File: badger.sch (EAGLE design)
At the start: 6 parts, among them U1 NCP1402

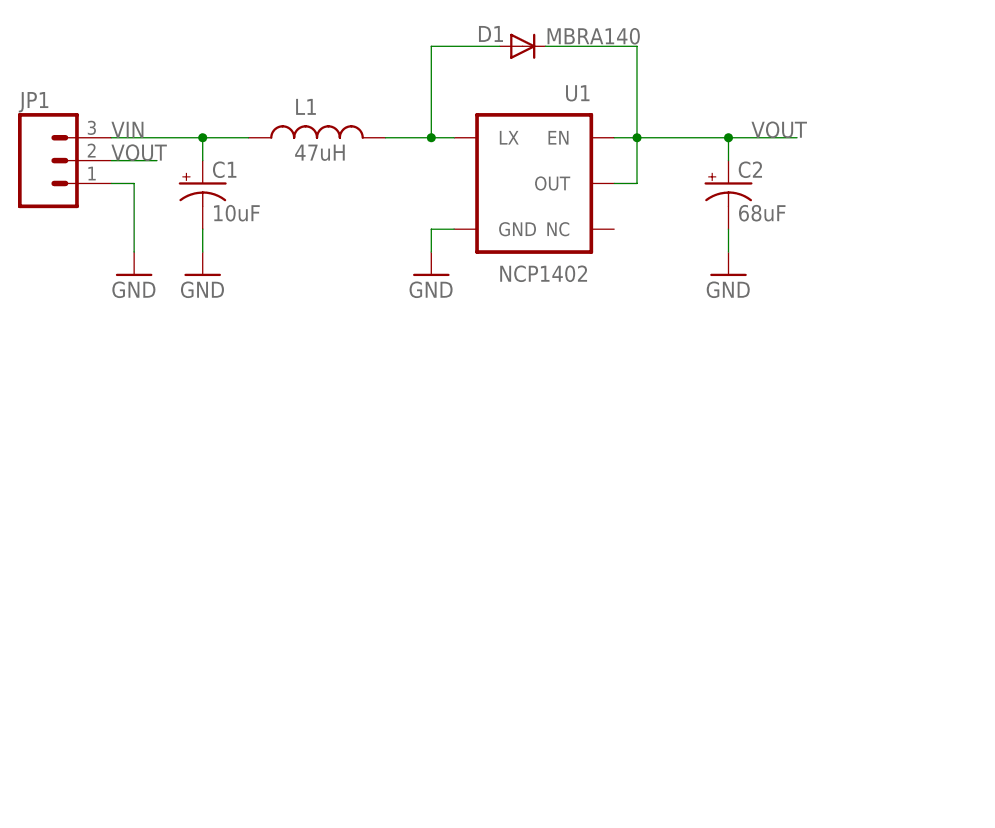
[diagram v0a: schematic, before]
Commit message: add esp8266 lib and add part
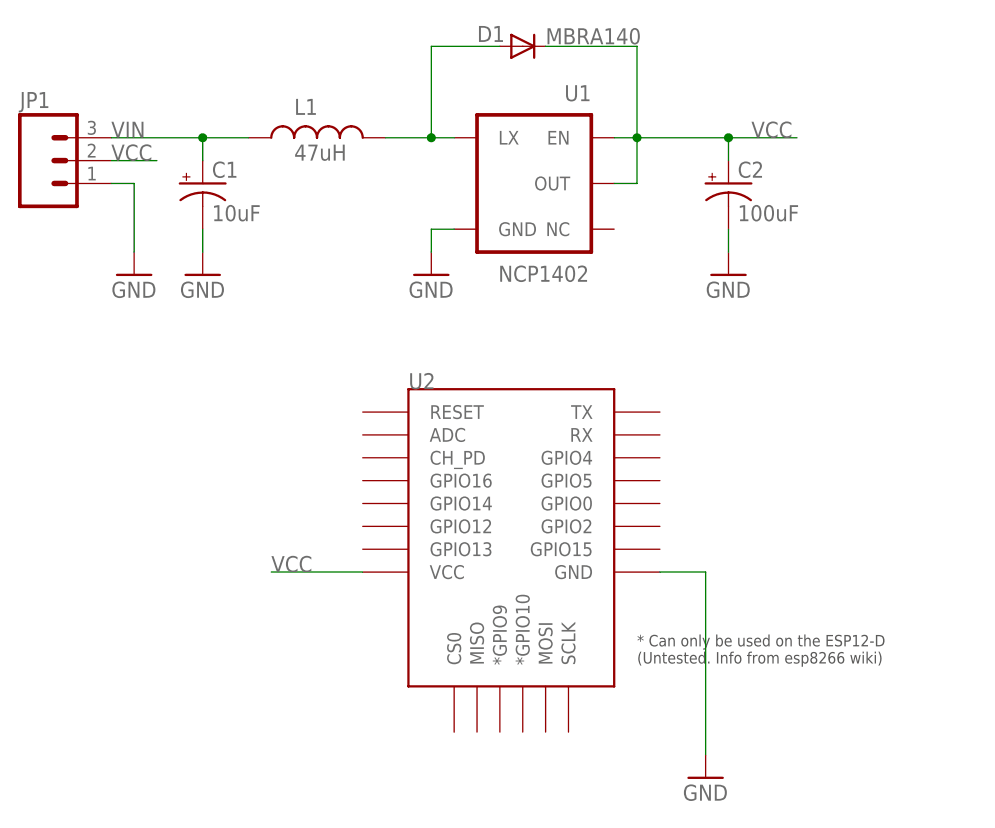
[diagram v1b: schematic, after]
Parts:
- added U2: (no value), esp8266modules:ESP12ESMD
- C2: value 68uF -> 100uF
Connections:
- removed net VOUT: C2.+, D1.C, JP1.2, U1.EN, U1.OUT
- new net VCC: C2.+, D1.C, JP1.2, U1.EN, U1.OUT, U2.VCC
- net GND: now also U2.GND
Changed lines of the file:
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@@
 <part name="D1" library="SparkFun" deviceset="DIODE" device="SMA" value="MBRA140"/>
 <part name="C1" library="SparkFun" deviceset="CAP_POL" device="1206" value="10uF"/>
-<part name="C2" library="SparkFun" deviceset="CAP_POL" device="3528" value="68uF"/>
+<part name="C2" library="SparkFun" deviceset="CAP_POL" device="3528" value="100uF"/>
 <part name="L1" library="SparkFun" deviceset="INDUCTOR" device="CR54" value="47uH"/>
 <part name="GND1" library="SparkFun" deviceset="GND" device=""/>
@@
 <part name="GND3" library="SparkFun" deviceset="GND" device=""/>
 <part name="GND4" library="SparkFun" deviceset="GND" device=""/>
+<part name="U2" library="esp8266modules" deviceset="ESP12E" device="SMD"/>
+<part name="GND5" library="SparkFun" deviceset="GND" device=""/>
 </parts>
 <sheets>
@@
 <instance part="GND3" gate="1" x="45.72" y="48.26"/>
 <instance part="GND4" gate="1" x="78.74" y="48.26"/>
+<instance part="U2" gate="G$1" x="55.88" y="25.4"/>
+<instance part="GND5" gate="1" x="76.2" y="-7.62"/>
 </instances>
 <busses>
@@
 <pinref part="D1" gate="G$1" pin="A"/>
 <pinref part="L1" gate="G$1" pin="2"/>
-</segment>
-</net>
-<net name="VOUT" class="0">
-<segment>
-<wire x1="66.04" y1="63.5" x2="68.58" y2="63.5" width="0.1524" layer="91"/>
-<wire x1="68.58" y1="63.5" x2="68.58" y2="58.42" width="0.1524" layer="91"/>
-<wire x1="68.58" y1="58.42" x2="66.04" y2="58.42" width="0.1524" layer="91"/>
-<wire x1="58.42" y1="73.66" x2="68.58" y2="73.66" width="0.1524" layer="91"/>
-<wire x1="68.58" y1="73.66" x2="68.58" y2="63.5" width="0.1524" layer="91"/>
-<wire x1="68.58" y1="63.5" x2="78.74" y2="63.5" width="0.1524" layer="91"/>
-<wire x1="78.74" y1="63.5" x2="78.74" y2="60.96" width="0.1524" layer="91"/>
-<wire x1="78.74" y1="63.5" x2="86.36" y2="63.5" width="0.1524" layer="91"/>
-<junction x="68.58" y="63.5"/>
-<junction x="78.74" y="63.5"/>
-<label x="81.28" y="63.5" size="1.778" layer="95"/>
-<pinref part="U1" gate="G$1" pin="EN"/>
-<pinref part="U1" gate="G$1" pin="OUT"/>
-<pinref part="D1" gate="G$1" pin="C"/>
-<pinref part="C2" gate="G$1" pin="+"/>
-</segment>
-<segment>
-<wire x1="10.16" y1="60.96" x2="15.24" y2="60.96" width="0.1524" layer="91"/>
-<label x="10.16" y="60.96" size="1.778" layer="95"/>
-<pinref part="JP1" gate="G$1" pin="2"/>
 </segment>
 </net>
@@
 <pinref part="GND1" gate="1" pin="GND"/>
 </segment>
+<segment>
+<pinref part="U2" gate="G$1" pin="GND"/>
+<pinref part="GND5" gate="1" pin="GND"/>
+<wire x1="71.12" y1="15.24" x2="76.2" y2="15.24" width="0.1524" layer="91"/>
+<wire x1="76.2" y1="15.24" x2="76.2" y2="-5.08" width="0.1524" layer="91"/>
+</segment>
 </net>
 <net name="VIN" class="0">
@@
 </segment>
 </net>
+<net name="VCC" class="0">
+<segment>
+<wire x1="66.04" y1="63.5" x2="68.58" y2="63.5" width="0.1524" layer="91"/>
+<wire x1="68.58" y1="63.5" x2="68.58" y2="58.42" width="0.1524" layer="91"/>
+<wire x1="68.58" y1="58.42" x2="66.04" y2="58.42" width="0.1524" layer="91"/>
+<wire x1="58.42" y1="73.66" x2="68.58" y2="73.66" width="0.1524" layer="91"/>
+<wire x1="68.58" y1="73.66" x2="68.58" y2="63.5" width="0.1524" layer="91"/>
+<wire x1="68.58" y1="63.5" x2="78.74" y2="63.5" width="0.1524" layer="91"/>
+<wire x1="78.74" y1="63.5" x2="78.74" y2="60.96" width="0.1524" layer="91"/>
+<wire x1="78.74" y1="63.5" x2="86.36" y2="63.5" width="0.1524" layer="91"/>
+<junction x="68.58" y="63.5"/>
+<junction x="78.74" y="63.5"/>
+<label x="81.28" y="63.5" size="1.778" layer="95"/>
+<pinref part="U1" gate="G$1" pin="EN"/>
+<pinref part="U1" gate="G$1" pin="OUT"/>
+<pinref part="D1" gate="G$1" pin="C"/>
+<pinref part="C2" gate="G$1" pin="+"/>
+</segment>
+<segment>
+<wire x1="10.16" y1="60.96" x2="15.24" y2="60.96" width="0.1524" layer="91"/>
+<label x="10.16" y="60.96" size="1.778" layer="95"/>
+<pinref part="JP1" gate="G$1" pin="2"/>
+</segment>
+<segment>
+<pinref part="U2" gate="G$1" pin="VCC"/>
+<wire x1="38.1" y1="15.24" x2="27.94" y2="15.24" width="0.1524" layer="91"/>
+<label x="27.94" y="15.24" size="1.778" layer="95"/>
+</segment>
+</net>
 </nets>
 </sheet>
@@
 </schematic>
 </drawing>
+<compatibility>
+<note version="6.3" minversion="6.2.2" severity="warning">
+Since Version 6.2.2 text objects can contain more than one line,
+which will not be processed correctly with this version.
+</note>
+</compatibility>
 </eagle>

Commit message: more updates
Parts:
- added GPIO15<->GND, GPIO16<->RESET: SOLDERJUMPERTRACE, SparkFun-Retired:SOLDERJUMPERTRACE
- added JP2, JP3: (no value), SparkFun-Connectors:M08
- added JP4: (no value), SparkFun-Connectors:M06SILK_FEMALE_PTH
- added R1: (no value), SparkFun-Resistors:RESISTOR-ARRAY0603-ARV
- added S1: RESET, SparkFun-Electromechanical:SWITCH-MOMENTARY-2SMD
- added S2: FLASH, SparkFun-Electromechanical:SWITCH-MOMENTARY-2SMD
- added S3: SWITCH-MOMENTARY-2SMD, SparkFun-Electromechanical:SWITCH-MOMENTARY-2SMD
- JP1: device SparkFun:M03PTH -> SparkFun-Connectors:ARDUINO_SERIAL_PROGRAMLOCK
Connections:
- new net 3.3V: C2.+, D1.C, R1A.1, R1D.2, U1.EN, U1.OUT
- new net ADC: JP2.7, U2.ADC
- new net CH_PD: JP1.CTS, JP2.6, R1D.1, U2.CH_PD
- new net CS0: JP4.1, U2.CS0
- new net GPIO0: JP1.DTR, JP3.5, R1A.2, S2.2, U2.GPIO0
- new net GPIO10: JP4.4, U2.*GPIO10
- new net GPIO12: JP2.3, U2.GPIO12
- new net GPIO13: JP2.2, U2.GPIO13
- new net GPIO14: JP2.4, U2.GPIO14
- new net GPIO15: GPIO15<->GND.1, JP3.7, U2.GPIO15
- new net GPIO16: GPIO16<->RESET.2, JP2.5, U2.GPIO16
- new net GPIO2: JP3.6
- new net GPIO4: JP3.3, U2.GPIO4
- new net GPIO5: JP3.4, U2.GPIO5
- new net GPIO9: JP4.3, U2.*GPIO9
- new net MISO: JP4.2, U2.MISO
- new net MOSI: JP4.5, U2.MOSI
- new net N$1: U2.GPIO2
- new net N$2: JP1.TXO
- new net N$4: JP1.RXI
- new net RESET: GPIO16<->RESET.1, JP2.8, S1.2, U2.RESET
- new net RX: JP3.2, U2.RX
- new net SCLK: JP4.6, U2.SCLK
- new net TX: JP3.1, U2.TX
- net GND: now also GPIO15<->GND.2, JP3.8, S1.1, S2.1; no longer JP1.1
- net VCC: now also JP1.VCC, JP2.1; no longer C2.+, D1.C, JP1.2, U1.EN, U1.OUT
- net VIN: no longer JP1.3
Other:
- note added: "TODO: BATTERY HOLDER FOOTPRINT LEDs CHEAP-O-CONFIGURATION POWER SWITCH RX<->TX SPEAKER USER BUTTON?"
- moved on the sheet: U2

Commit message: some updates
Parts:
- removed S3: SWITCH-MOMENTARY-2SMD, SparkFun-Electromechanical:SWITCH-MOMENTARY-2SMD
- added CHEAPO-1, CHEAPO-2, CHEAPO-3: (no value), SparkFun-Retired:SOLDERJUMPER_2WAYT
- added D2, D3, D4: (no value), SparkFun-LED:LED-3MM-NO_SILK
- added R2, R3, R4: 100, SparkFun-Resistors:RESISTOR1206
- added R5: 500K, SparkFun-Resistors:RESISTOR0603
- added R6: 250K, SparkFun-Resistors:RESISTOR0603
- added U$1: BATTERY, badger:BATTERY
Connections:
- new net N$10: CHEAPO-3.2, R4.2
- new net N$11: CHEAPO-1.2, R2.2
- new net N$15: CHEAPO-2.2, R3.2
- new net N$5: D2.A, R2.1
- new net N$6: D3.A, R3.1
- new net N$7: D4.A, R4.1
- net 3.3V: now also R1R.1
- net ADC: now also R5.1, R6.2
- net GND: now also D2.C, D3.C, D4.C, R1B.2, R6.1, U$1.-; no longer GPIO15<->GND.2
- net GPIO12: now also CHEAPO-1.3
- net GPIO13: now also CHEAPO-2.3
- net GPIO15: now also CHEAPO-3.3
- net GPIO2: now also R1R.2, U2.GPIO2
- net N$1: now also GPIO15<->GND.2, R1B.1; no longer U2.GPIO2
- net VIN: now also CHEAPO-1.1, CHEAPO-2.1, CHEAPO-3.1, R5.2, U$1.+
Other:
- note added: "TODO: RGB LED CHEAP-O-CONFIGURATION POWER SWITCH"
- note removed: "TODO: BATTERY HOLDER FOOTPRINT LEDs CHEAP-O-CONFIGURATION POWER SWITCH RX<->TX SPEAKER USER BUTTON?"
- moved on the sheet: R1B, R1R

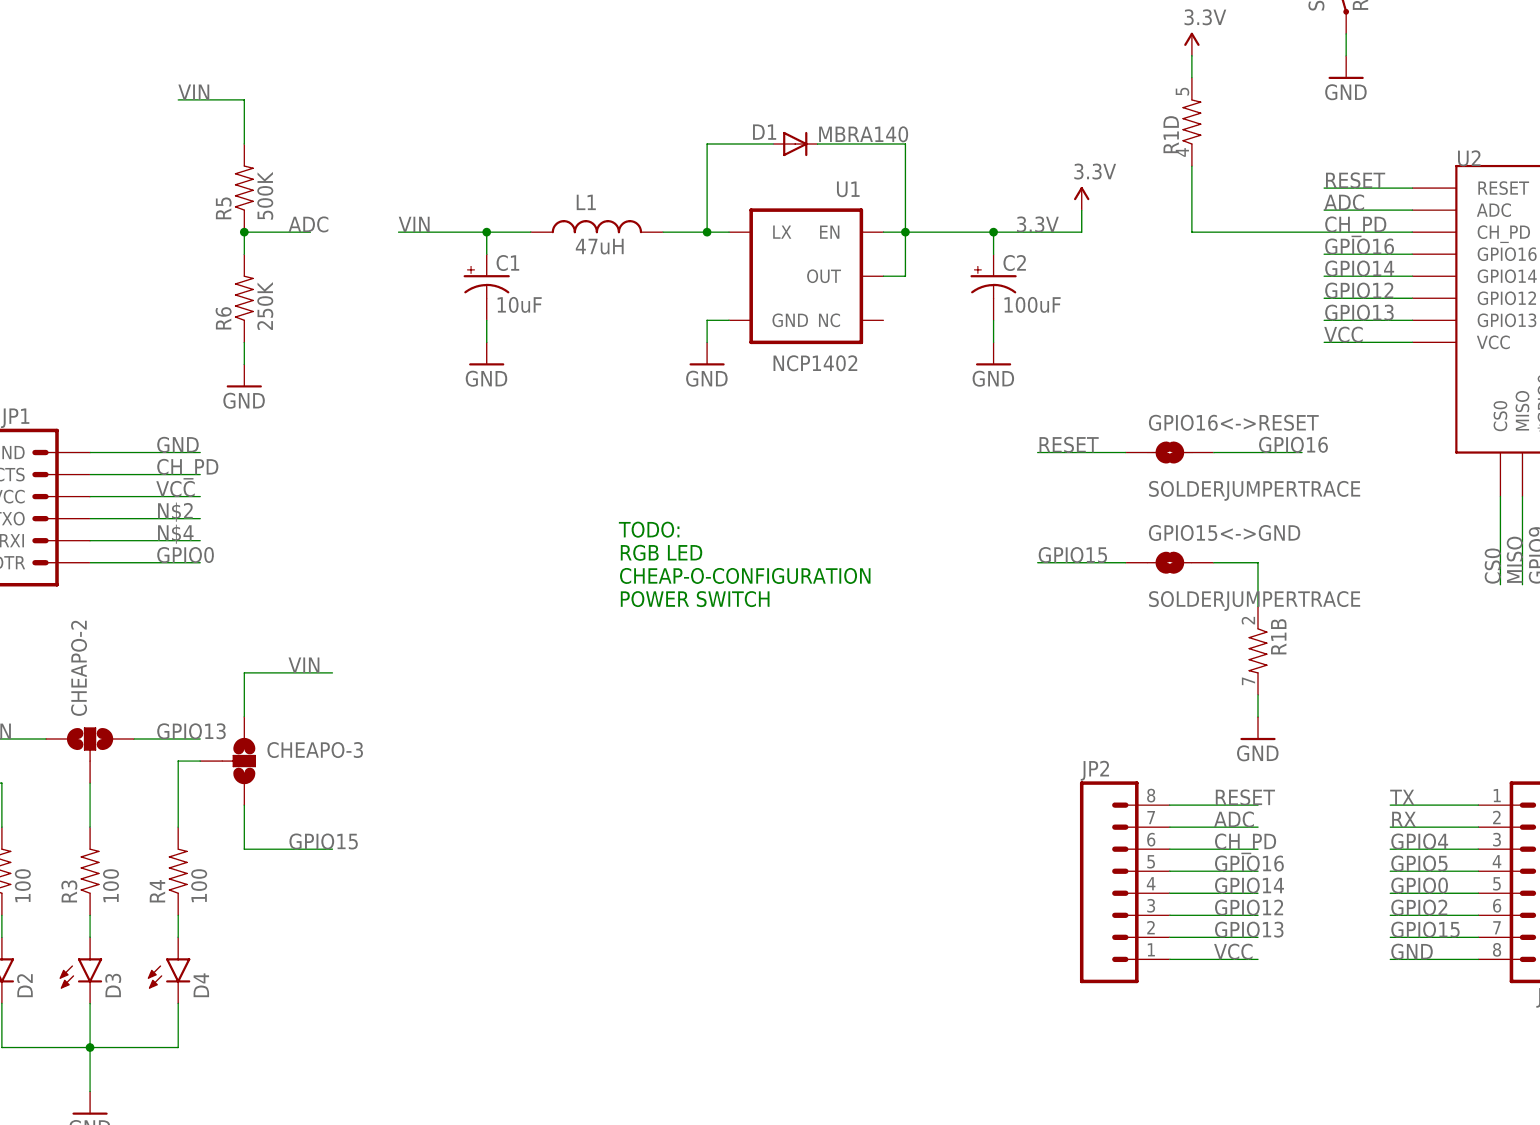
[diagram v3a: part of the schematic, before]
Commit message: add switch and associated scripting
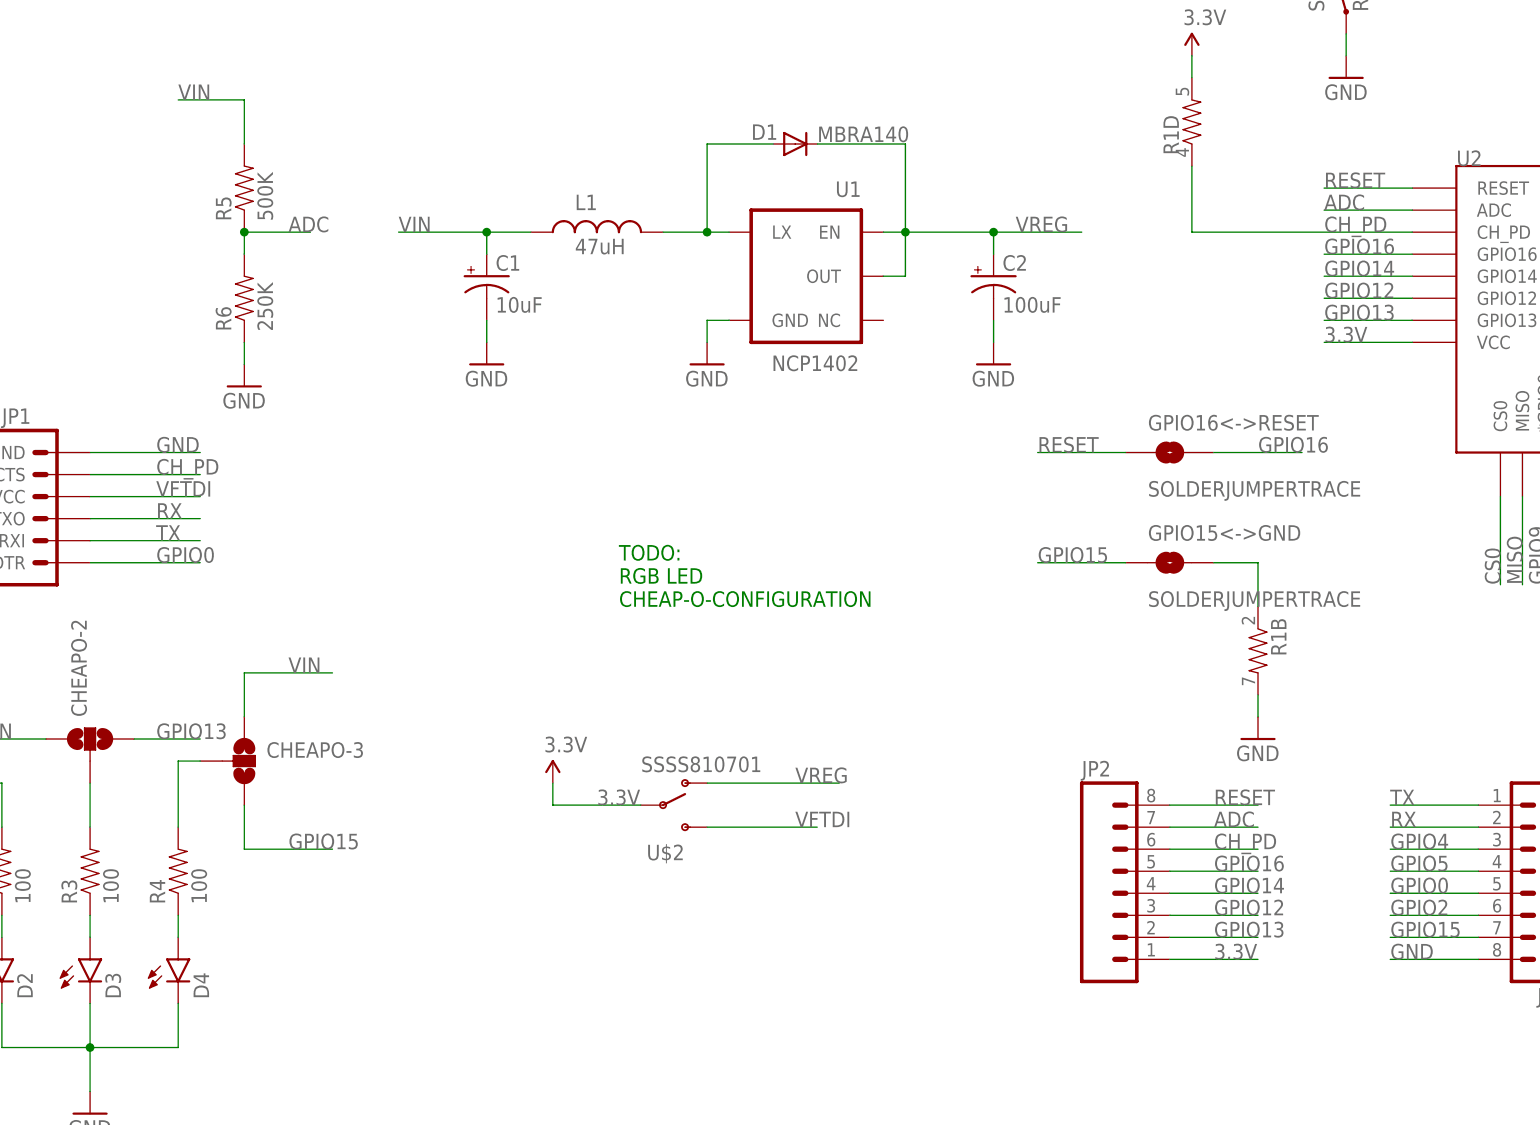
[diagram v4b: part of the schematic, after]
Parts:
- added U$2: SSSS810701, badger:SSSS810701
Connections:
- removed net N$2: JP1.TXO
- removed net N$4: JP1.RXI
- removed net VCC: JP1.VCC, JP2.1, U2.VCC
- new net VFTDI: JP1.VCC, U$2.S
- new net VREG: C2.+, D1.C, U$2.O, U1.EN, U1.OUT
- net 3.3V: now also JP2.1, U$2.P, U2.VCC; no longer C2.+, D1.C, U1.EN, U1.OUT
- net RX: now also JP1.TXO
- net TX: now also JP1.RXI
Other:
- note added: "TODO: RGB LED CHEAP-O-CONFIGURATION"
- note removed: "TODO: RGB LED CHEAP-O-CONFIGURATION POWER SWITCH"

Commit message: updates to schematic
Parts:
- removed R2, R3, R4: 100, SparkFun-Resistors:RESISTOR1206
- added CHEAPO-4, CHEAPO-5, CHEAPO-6, CHEAPO-7: (no value), SparkFun-Retired:SOLDERJUMPER_2WAYT
- added D5: FZR50RGB00T-C, Seeed-OPL-Diode:DIP-LED-RGB-COMMON-ANODE(4P-D5MM)
- added D6: (no value), SparkFun-LED:LED-3MM-NO_SILK
- added Q1: MOSFET-NCHANNEL2N7002PW, SparkFun-DiscreteSemi:MOSFET-NCHANNEL2N7002PW
- added R10: 100, SparkFun-Resistors:RESISTOR-ARRAY0603-ARV
- added R7, R8, R9: 100, SparkFun-Resistors:RESISTOR1206
- added U$3: PS603SPK, adafruit:PS603SPK
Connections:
- removed net N$10: CHEAPO-3.2, R4.2
- new net N$12: CHEAPO-5.2, R8.1
- new net N$13: CHEAPO-3.2, R10B.2
- new net N$14: CHEAPO-2.2, R10R.2
- new net N$16: CHEAPO-7.2, R10A.2
- new net N$17: CHEAPO-6.2, R9.1
- new net N$18: Q1.S, U$3.1
- new net N$2: D5.R, R8.2
- new net N$4: D5.G, R7.2
- new net N$8: D5.B, R9.2
- new net N$9: CHEAPO-4.2, R7.1
- net 3.3V: now also D5.+
- net GND: now also CHEAPO-4.3, CHEAPO-5.3, CHEAPO-6.3, D6.C, Q1.D
- net GPIO0: now also CHEAPO-7.3
- net GPIO12: now also CHEAPO-4.1; no longer CHEAPO-1.3
- net GPIO13: now also CHEAPO-5.1; no longer CHEAPO-2.3
- net GPIO14: now also CHEAPO-1.3
- net GPIO15: now also CHEAPO-6.1; no longer CHEAPO-3.3
- net GPIO16: now also Q1.G
- net GPIO4: now also CHEAPO-2.3
- net GPIO5: now also CHEAPO-3.3
- net N$11: now also D6.A, R10A.1; no longer CHEAPO-1.2, R2.2
- net N$15: now also CHEAPO-1.2, R10D.2; no longer CHEAPO-2.2, R3.2
- net N$5: now also R10B.1; no longer R2.1
- net N$6: now also R10R.1; no longer R3.1
- net N$7: now also R10D.1; no longer R4.1
- net VIN: now also CHEAPO-7.1, U$3.2
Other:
- note added: "TODO: SPEAKER"
- note removed: "TODO: RGB LED CHEAP-O-CONFIGURATION"
- moved on the sheet: CHEAPO-1, CHEAPO-2, CHEAPO-3, D2, D3, D4

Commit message: outline, but hit the limits of eagle free
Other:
- note removed: "TODO: SPEAKER"
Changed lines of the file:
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@@
 <sheet>
 <plain>
-<text x="35.56" y="20.32" size="1.778" layer="91">TODO:
-SPEAKER
-</text>
 </plain>
 <instances>
